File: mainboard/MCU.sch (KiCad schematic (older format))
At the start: 55 parts, among them J9 Micro_SD_Card_Det_Hirose_DM3AT, SW1 RESET, U11 STM32G474R, U12 M95256-WMN6P, U17 CD74HC4067SM, U5 MCP2562, U6 LM358

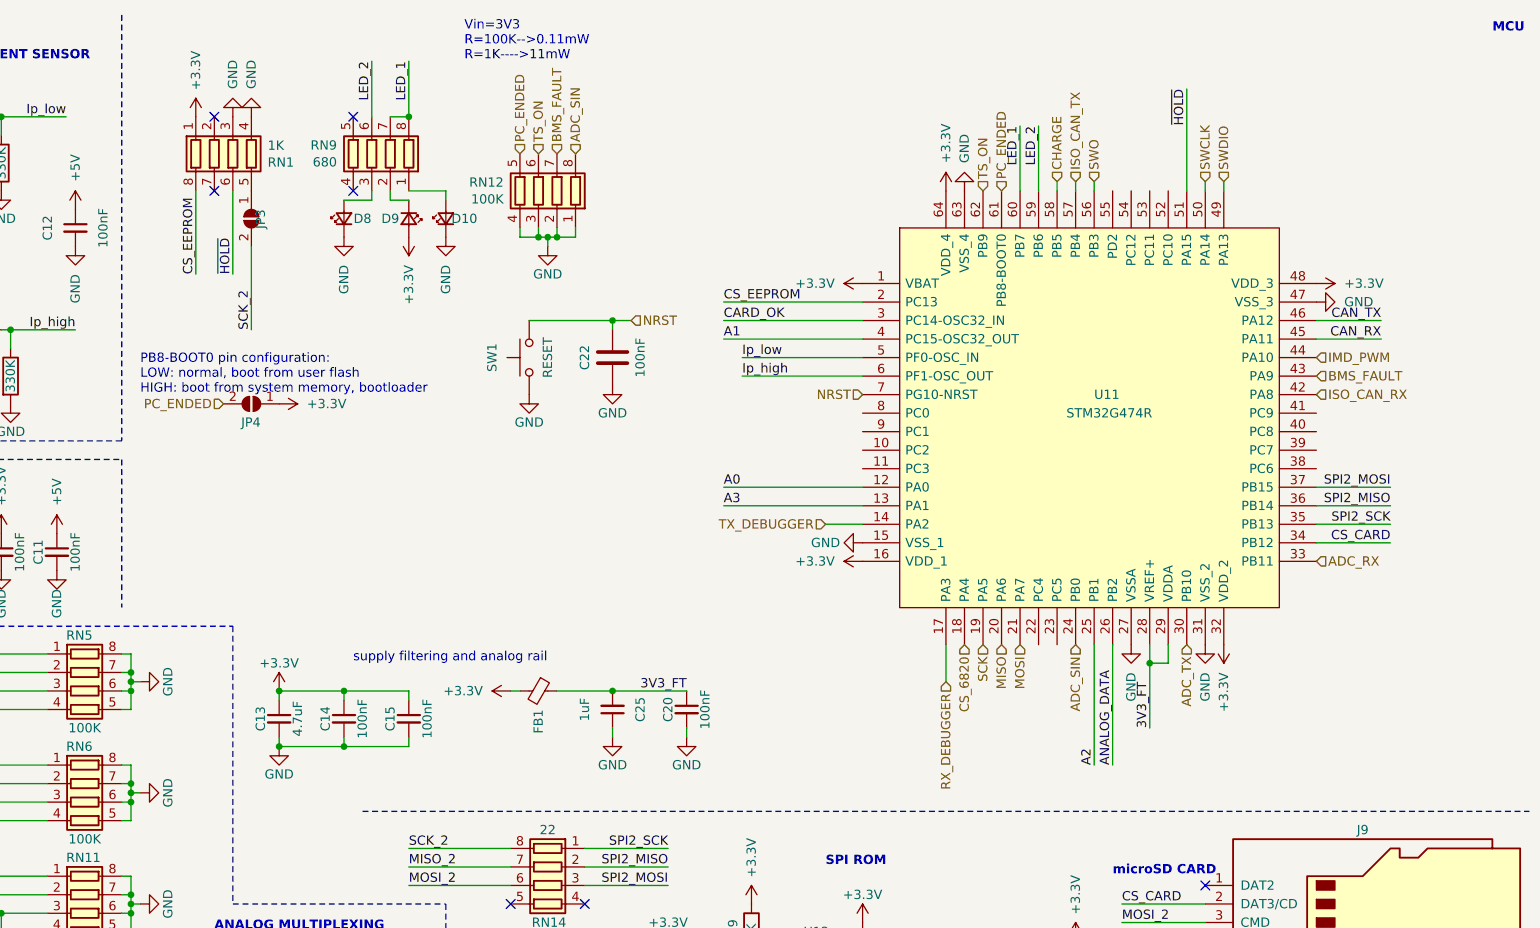
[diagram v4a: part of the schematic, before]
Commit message: 64pin, testpoints, commenting, general refactoring
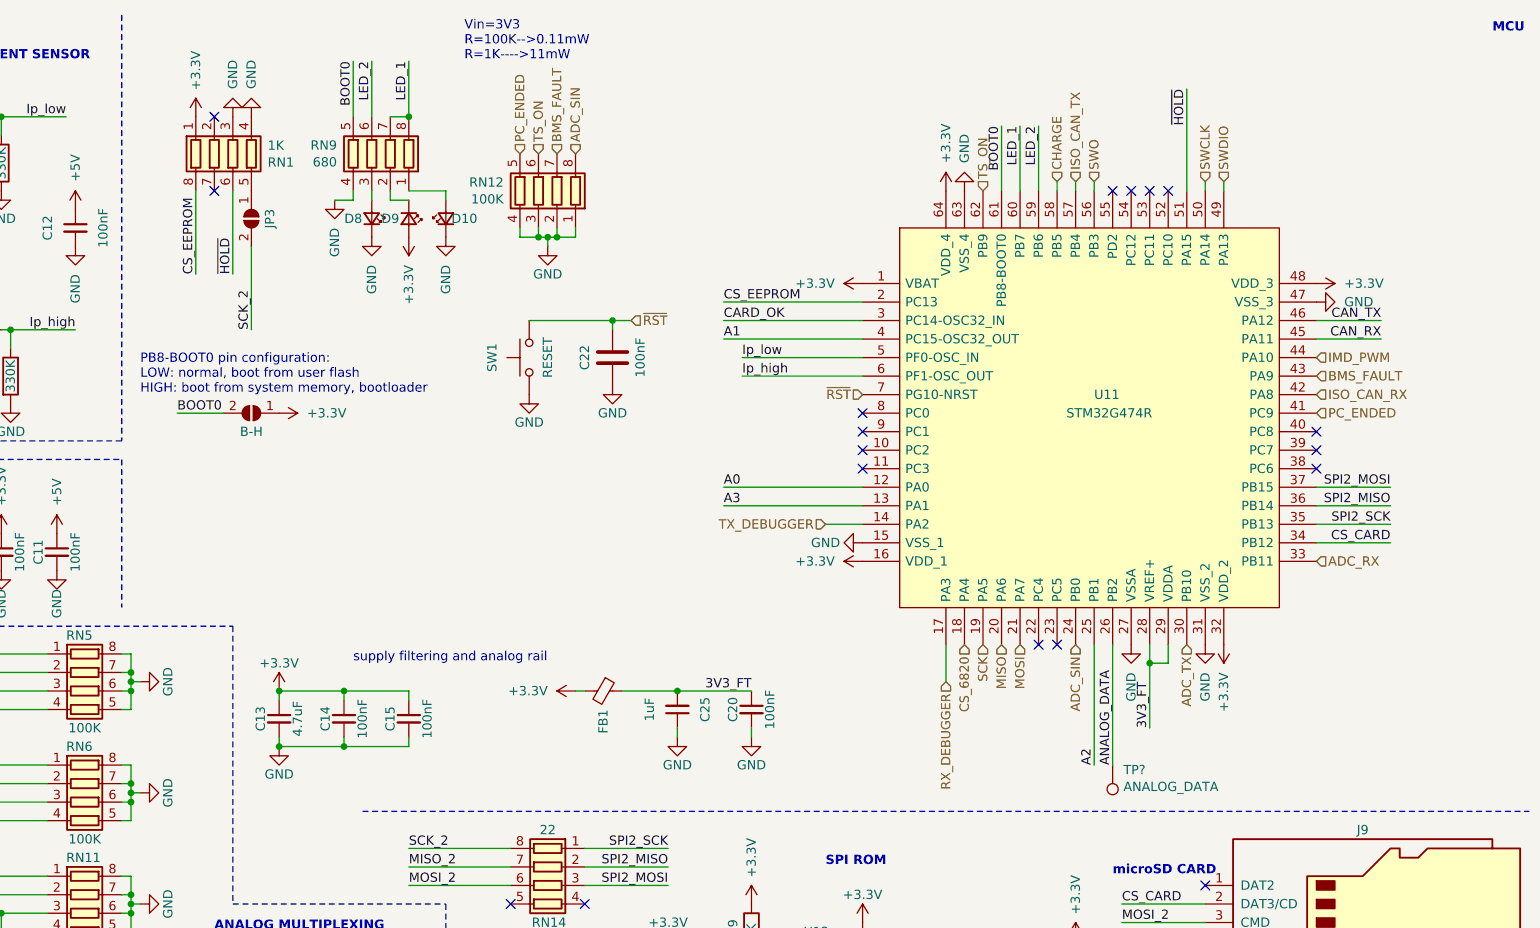
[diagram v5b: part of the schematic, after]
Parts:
- added TP?: ANALOG_DATA, symbol Connector:TestPoint
- renumbered JP4 to B-H
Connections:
- net ANALOG_DATA: now also TP?.1
- net GND: now also RN9.4 (R4.1)
- net PC_ENDED: now also U11.41 (PC9); no longer B-H.2 (B), U11.61 (PB8-BOOT0)
- net BOOT0: now reaches RN9.5 (R4.2)
- net BOOT0: now also B-H.2 (B), U11.61 (PB8-BOOT0)
- net NRST renamed ~RST~
- no-connect marks 10 -> 21
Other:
- moved on the sheet: B-H, C20, C25, D8, FB1
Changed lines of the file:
@@
 L Device:C_Small C?
 U 1 1 5E1247F7
-P 6650 4250
+P 7000 4250
 AR Path="/5E1247F7" Ref="C?"  Part="1"
 AR Path="/5DF398FB/5E1247F7" Ref="C20"  Part="1"
-F 0 "C20" V 6550 4250 50  0000 C CNN
-F 1 "100nF" V 6750 4250 50  0000 C CNN
-F 2 "Capacitor_SMD:C_0603_1608Metric" H 6688 4100 50  0001 C CNN
-F 3 "~" H 6650 4250 50  0001 C CNN
-	1    6650 4250
+F 0 "C20" V 6900 4250 50  0000 C CNN
+F 1 "100nF" V 7100 4250 50  0000 C CNN
+F 2 "Capacitor_SMD:C_0603_1608Metric" H 7038 4100 50  0001 C CNN
+F 3 "~" H 7000 4250 50  0001 C CNN
+	1    7000 4250
 	1    0    0    -1
 $EndComp
@@
 L power:GND #PWR?
 U 1 1 5DF87343
-P 6250 4400
+P 6600 4400
 AR Path="/5DF87343" Ref="#PWR?"  Part="1"
 AR Path="/5DF398FB/5DF87343" Ref="#PWR0110"  Part="1"
-F 0 "#PWR0110" H 6250 4150 50  0001 C CNN
-F 1 "GND" H 6250 4250 50  0000 C CNN
-F 2 "" H 6250 4400 50  0001 C CNN
-F 3 "" H 6250 4400 50  0001 C CNN
-	1    6250 4400
+F 0 "#PWR0110" H 6600 4150 50  0001 C CNN
+F 1 "GND" H 6600 4250 50  0000 C CNN
+F 2 "" H 6600 4400 50  0001 C CNN
+F 3 "" H 6600 4400 50  0001 C CNN
+	1    6600 4400
 	1    0    0    -1
 $EndComp
@@
 L Device:C_Small C?
 U 1 1 5DF87349
-P 6250 4250
+P 6600 4250
 AR Path="/5DF87349" Ref="C?"  Part="1"
 AR Path="/5DF398FB/5DF87349" Ref="C25"  Part="1"
-F 0 "C25" V 6100 4250 50  0000 C CNN
-F 1 "1uF" V 6400 4250 50  0000 C CNN
-F 2 "Capacitor_SMD:C_0603_1608Metric" H 6288 4100 50  0001 C CNN
-F 3 "~" H 6250 4250 50  0001 C CNN
-	1    6250 4250
+F 0 "C25" V 6450 4250 50  0000 C CNN
+F 1 "1uF" V 6750 4250 50  0000 C CNN
+F 2 "Capacitor_SMD:C_0603_1608Metric" H 6638 4100 50  0001 C CNN
+F 3 "~" H 6600 4250 50  0001 C CNN
+	1    6600 4250
 	-1   0    0    1
 $EndComp
@@
 L power:+3.3V #PWR?
 U 1 1 5E60753C
-P 5700 4150
+P 6050 4150
 AR Path="/5E60753C" Ref="#PWR?"  Part="1"
 AR Path="/5DF398FB/5E60753C" Ref="#PWR0118"  Part="1"
-F 0 "#PWR0118" H 5700 4000 50  0001 C CNN
-F 1 "+3.3V" V 5700 4300 50  0000 L CNN
-F 2 "" H 5700 4150 50  0001 C CNN
-F 3 "" H 5700 4150 50  0001 C CNN
-	1    5700 4150
+F 0 "#PWR0118" H 6050 4000 50  0001 C CNN
+F 1 "+3.3V" V 6050 4300 50  0000 L CNN
+F 2 "" H 6050 4150 50  0001 C CNN
+F 3 "" H 6050 4150 50  0001 C CNN
+	1    6050 4150
 	0    -1   -1   0
 $EndComp
@@
 L Device:FerriteBead_Small FB1
 U 1 1 5E60756E
-P 5850 4150
-F 0 "FB1" H 5950 4150 50  0000 L CNN
-F 1 "FerriteBead_Small" H 5950 4105 50  0001 L CNN
-F 2 "Inductor_SMD:L_0603_1608Metric_Pad1.05x0.95mm_HandSolder" V 5780 4150 50  0001 C CNN
-F 3 "~" H 5850 4150 50  0001 C CNN
-	1    5850 4150
+P 6200 4150
+F 0 "FB1" H 6300 4150 50  0000 L CNN
+F 1 "FerriteBead_Small" H 6300 4105 50  0001 L CNN
+F 2 "Inductor_SMD:L_0603_1608Metric_Pad1.05x0.95mm_HandSolder" V 6130 4150 50  0001 C CNN
+F 3 "~" H 6200 4150 50  0001 C CNN
+	1    6200 4150
 	0    1    1    0
 $EndComp
 Wire Wire Line
-	5950 4150 6250 4150
-Wire Wire Line
-	6250 4150 6650 4150
-Wire Wire Line
-	5700 4150 5750 4150
-Wire Wire Line
-	6250 4350 6250 4400
-Text Label 6650 4150 2    50   ~ 0
+	6300 4150 6600 4150
+Wire Wire Line
+	6600 4150 7000 4150
+Wire Wire Line
+	6050 4150 6100 4150
+Wire Wire Line
+	6600 4350 6600 4400
+Text Label 7000 4150 2    50   ~ 0
 3V3_FT
-Connection ~ 6250 4150
+Connection ~ 6600 4150
 Wire Wire Line
 	10050 2250 10400 2250
@@
 L power:GND #PWR?
 U 1 1 5E572A92
-P 6650 4400
+P 7000 4400
 AR Path="/5E572A92" Ref="#PWR?"  Part="1"
 AR Path="/5DF398FB/5E572A92" Ref="#PWR0103"  Part="1"
-F 0 "#PWR0103" H 6650 4150 50  0001 C CNN
-F 1 "GND" H 6650 4250 50  0000 C CNN
-F 2 "" H 6650 4400 50  0001 C CNN
-F 3 "" H 6650 4400 50  0001 C CNN
-	1    6650 4400
-	1    0    0    -1
-$EndComp
-Wire Wire Line
-	6650 4350 6650 4400
+F 0 "#PWR0103" H 7000 4150 50  0001 C CNN
+F 1 "GND" H 7000 4250 50  0000 C CNN
+F 2 "" H 7000 4400 50  0001 C CNN
+F 3 "" H 7000 4400 50  0001 C CNN
+	1    7000 4400
+	1    0    0    -1
+$EndComp
+Wire Wire Line
+	7000 4350 7000 4400
 Text HLabel 8250 1450 1    50   Input ~ 0
 TS_ON
@@
 L power:GND #PWR?
 U 1 1 5E86FDC4
-P 4800 1700
+P 4950 1700
 AR Path="/5E86FDC4" Ref="#PWR?"  Part="1"
 AR Path="/5DF398FB/5E86FDC4" Ref="#PWR0157"  Part="1"
-F 0 "#PWR0157" H 4800 1450 50  0001 C CNN
-F 1 "GND" V 4800 1550 50  0000 R CNN
-F 2 "" H 4800 1700 50  0001 C CNN
-F 3 "" H 4800 1700 50  0001 C CNN
-	1    4800 1700
-	1    0    0    -1
+F 0 "#PWR0157" H 4950 1450 50  0001 C CNN
+F 1 "GND" V 4950 1550 50  0000 R CNN
+F 2 "" H 4950 1700 50  0001 C CNN
+F 3 "" H 4950 1700 50  0001 C CNN
+	1    4950 1700
+	-1   0    0    -1
 $EndComp
 $Comp
 L Device:LED_Small D?
 U 1 1 5E86FDCA
-P 4800 1600
+P 4950 1600
 AR Path="/5E86FDCA" Ref="D?"  Part="1"
 AR Path="/5DF398FB/5E86FDCA" Ref="D8"  Part="1"
-F 0 "D8" V 4800 1500 50  0000 C CNN
-F 1 "LED_Small" H 4800 1744 50  0001 C CNN
-F 2 "MainBoard:LED_REVERSE_MOUNT_cilindrical" V 4800 1600 50  0001 C CNN
-F 3 "~" V 4800 1600 50  0001 C CNN
-	1    4800 1600
-	0    -1   -1   0
+F 0 "D8" V 4950 1500 50  0000 C CNN
+F 1 "LED_Small" H 4950 1744 50  0001 C CNN
+F 2 "MainBoard:LED_REVERSE_MOUNT_cilindrical" V 4950 1600 50  0001 C CNN
+F 3 "~" V 4950 1600 50  0001 C CNN
+	1    4950 1600
+	0    1    -1   0
 $EndComp
 Wire Wire Line
@@
 Wire Wire Line
 	4950 750  4950 1050
-NoConn ~ 4850 1050
-NoConn ~ 4850 1450
 $Comp
 L Device:R R?
@@
 U 1 1 5EB0119F
 P 4300 1600
-F 0 "JP3" H 4250 1550 50  0000 L CNN
+F 0 "JP3" H 4300 1500 50  0000 C CNN
 F 1 "SolderJumper_2_Open" V 4345 1648 50  0001 L CNN
 F 2 "MainBoard:Jumper_SMD_0603" H 4300 1600 50  0001 C CNN
@@
 	0    1    1    0
 $EndComp
-Wire Wire Line
-	4800 1500 4950 1500
 Wire Wire Line
 	4950 1500 4950 1450
@@
 Text Notes 3700 2550 0    50   ~ 0
 PB8-BOOT0 pin configuration:\nLOW: normal, boot from user flash\nHIGH: boot from system memory, bootloader
-Text HLabel 4150 2600 0    50   Input ~ 0
-PC_ENDED
 $Comp
 L power:+3.3V #PWR?
 U 1 1 5FD436DF
-P 4450 2600
+P 4450 2650
 AR Path="/5FD436DF" Ref="#PWR?"  Part="1"
 AR Path="/5DF398FB/5FD436DF" Ref="#PWR016"  Part="1"
-F 0 "#PWR016" H 4450 2450 50  0001 C CNN
-F 1 "+3.3V" V 4450 2750 50  0000 L CNN
-F 2 "" H 4450 2600 50  0001 C CNN
-F 3 "" H 4450 2600 50  0001 C CNN
-	1    4450 2600
+F 0 "#PWR016" H 4450 2500 50  0001 C CNN
+F 1 "+3.3V" V 4450 2800 50  0000 L CNN
+F 2 "" H 4450 2650 50  0001 C CNN
+F 3 "" H 4450 2650 50  0001 C CNN
+	1    4450 2650
 	0    1    1    0
 $EndComp
 $Comp
-L Jumper:SolderJumper_2_Open JP4
+L Jumper:SolderJumper_2_Open B-H
 U 1 1 5FD45CCD
-P 4300 2600
-F 0 "JP4" H 4250 2500 50  0000 L CNN
-F 1 "SolderJumper_2_Open" V 4345 2648 50  0001 L CNN
-F 2 "MainBoard:Jumper_SMD_0603" H 4300 2600 50  0001 C CNN
-F 3 "~" H 4300 2600 50  0001 C CNN
-	1    4300 2600
+P 4300 2650
+F 0 "B-H" H 4300 2550 50  0000 C CNN
+F 1 "SolderJumper_2_Open" V 4345 2698 50  0001 L CNN
+F 2 "MainBoard:Jumper_SMD_0603" H 4300 2650 50  0001 C CNN
+F 3 "~" H 4300 2650 50  0001 C CNN
+	1    4300 2650
 	-1   0    0    -1
 $EndComp
@@
 Wire Wire Line
 	8750 1400 8750 1450
-Text HLabel 8350 1450 1    50   Input ~ 0
+Text HLabel 10050 2650 2    50   Input ~ 0
 PC_ENDED
 Text Label 9350 900  3    50   ~ 0
@@
 $EndComp
 Text HLabel 6350 2150 2    50   Input ~ 0
-NRST
+~RST~
 Wire Wire Line
 	6250 2150 6350 2150
 Connection ~ 6250 2150
 Text HLabel 7600 2550 0    50   Input ~ 0
-NRST
+~RST~
 Text Label 10450 3350 2    50   ~ 0
 CS_CARD
@@
 Text Notes 7000 6650 0    50   ~ 0
 AMS: Automatic Moaning System
+Text Label 8350 1100 3    50   ~ 0
+BOOT0
+Wire Wire Line
+	8350 1100 8350 1450
+NoConn ~ 8950 1450
+NoConn ~ 9050 1450
+NoConn ~ 9150 1450
+NoConn ~ 9250 1450
+NoConn ~ 7600 2650
+NoConn ~ 7600 2750
+NoConn ~ 7600 2850
+NoConn ~ 7600 2950
+NoConn ~ 8550 3900
+NoConn ~ 8650 3900
+NoConn ~ 10050 2950
+NoConn ~ 10050 2750
+NoConn ~ 10050 2850
+Text Label 3900 2650 0    50   ~ 0
+BOOT0
+Wire Wire Line
+	3900 2650 4150 2650
+Text Label 4850 750  3    50   ~ 0
+BOOT0
+Wire Wire Line
+	4850 750  4850 1050
+$Comp
+L power:GND #PWR?
+U 1 1 6057F2A0
+P 4750 1500
+AR Path="/6057F2A0" Ref="#PWR?"  Part="1"
+AR Path="/5DF398FB/6057F2A0" Ref="#PWR?"  Part="1"
+F 0 "#PWR?" H 4750 1250 50  0001 C CNN
+F 1 "GND" V 4750 1350 50  0000 R CNN
+F 2 "" H 4750 1500 50  0001 C CNN
+F 3 "" H 4750 1500 50  0001 C CNN
+	1    4750 1500
+	-1   0    0    -1
+$EndComp
+Wire Wire Line
+	4750 1500 4850 1500
+Wire Wire Line
+	4850 1500 4850 1450
+$Comp
+L Connector:TestPoint TP?
+U 1 1 60590C21
+P 8950 4550
+F 0 "TP?" H 8892 4576 50  0000 R CNN
+F 1 "ANALOG_DATA" H 8892 4667 50  0000 R CNN
+F 2 "" H 9150 4550 50  0001 C CNN
+F 3 "~" H 9150 4550 50  0001 C CNN
+	1    8950 4550
+	-1   0    0    1
+$EndComp
 $EndSCHEMATC

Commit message: updated libraries
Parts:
- FB1: symbol Device:FerriteBead_Small -> Device:Ferrite_Bead_Small
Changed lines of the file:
@@
 $EndComp
 $Comp
-L Device:FerriteBead_Small FB1
+L Device:Ferrite_Bead_Small FB1
 U 1 1 5E60756E
 P 6200 4150
+AR Path="/5E60756E" Ref="FB1"  Part="1"
+AR Path="/5DF398FB/5E60756E" Ref="FB1"  Part="1"
 F 0 "FB1" H 6300 4150 50  0000 L CNN
 F 1 "FerriteBead_Small" H 6300 4105 50  0001 L CNN

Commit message: v1.1 as printed
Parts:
- removed C29: 100nF, Capacitor_SMD:C_0603_1608Metric, symbol Device:C_Small
- removed D5, D6, D7: 3V, Diode_SMD:D_SOD-323, symbol Device:D_Zener_Small
- removed R14, R15, R16: 1M, Resistor_SMD:R_0603_1608Metric, symbol Device:R
- removed R19, R20: 2K, Resistor_SMD:R_0603_1608Metric, symbol Device:R
- removed R30: 100K, Resistor_SMD:R_0603_1608Metric, symbol Device:R
- removed RN10, RN11, RN5, RN6, RN7: 100K, MainBoard:R_network_4x1_bourns_CAY16, symbol Device:R_Pack04
- removed RN14: 22, MainBoard:R_network_4x1_bourns_CAY16, symbol Device:R_Pack04
- removed RN2, RN3, RN4: 330K, MainBoard:R_network_4x1_bourns_CAY16, symbol Device:R_Pack04
- removed TP?: ANALOG_DATA, symbol Connector:TestPoint
- removed U11: STM32G474R, Package_QFP:LQFP-64_10x10mm_P0.5mm, symbol MainBoard:STM32G474R
- removed U17: CD74HC4067SM, Package_SO:TSSOP-24_4.4x7.8mm_P0.65mm, symbol 74xx:CD74HC4067SM
- added C19, C21: 1uF, Capacitor_SMD:C_0805_2012Metric, symbol Device:C_Small
- added C38, C39: 20pF, Capacitor_SMD:C_0603_1608Metric, symbol Device:C_Small
- added C48: 100nF, Capacitor_SMD:C_0603_1608Metric, symbol Device:C_Small
- added J12: SPARE_PINS, Connector_PinHeader_2.54mm:PinHeader_2x05_P2.54mm_Vertical, symbol Connector_Generic:Conn_02x05_Odd_Even
- added R6: 10K, Resistor_SMD:R_0603_1608Metric, symbol Device:R
- added RN14, RN22: 22, MainBoard:R_network_4x1_bourns_CAY16, symbol Device:R_Pack04_Split
- added TP15: Ip_high, TestPoint:TestPoint_Pad_D1.0mm, symbol Connector:TestPoint
- added TP16: BMS_FAULT, TestPoint:TestPoint_Pad_D1.0mm, symbol Connector:TestPoint
- added TP33: VCAP, TestPoint:TestPoint_Pad_D1.0mm, symbol Connector:TestPoint
- added TP9: Ip_low, TestPoint:TestPoint_Pad_D1.0mm, symbol Connector:TestPoint
- added U9: STM32F446RE_64PIN, Package_QFP:LQFP-64_10x10mm_P0.5mm, symbol MainBoard:STM32F446RE_64PIN
- added Y1: 26MHz, Crystal:Crystal_SMD_3225-4Pin_3.2x2.5mm, symbol Device:Crystal_GND24_Small
- B-H1: renamed from B-H; value SolderJumper_2_Open -> BOOT0
- C25: footprint Capacitor_SMD:C_0603_1608Metric -> Capacitor_SMD:C_0805_2012Metric
- J9: footprint MainBoard:MicroSD_Hirose_DM3AT-SF-PEJM5 -> Connector_Card:microSD_HC_Hirose_DM3AT-SF-PEJM5
- JP3: footprint MainBoard:Jumper_SMD_0603 -> Jumper:SolderJumper-2_P1.3mm_Open_RoundedPad1.0x1.5mm
- RN1: value 1K -> 100K
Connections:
- net PC_ENDED is gone; now on net BOOT0: RN12.5 (R4.2)
- net +3V3: now also RN1.2 (R2.1), C48.1, R6.1, U9.1 (VBAT), U9.19 (VDD), U9.32 (VDD), U9.48 (VDD), U9.64 (VDD)
- net 3V3_FT: now also U9.13 (VDDA)
- net ADC_RX: now also U9.25 (PC5)
- net ADC_SIN: now also U9.26 (PB0)
- net ADC_TX: now also U9.29 (PB10)
- net BMS_FAULT: now also TP16.1, U9.51 (PC10)
- net BOOT0: now also U9.60 (BOOT0); no longer RN9.5 (R4.2)
- net CAN_RX: now also RN22.5 (R4.2), U9.57 (PB5); no longer U5.4 (RXD)
- net CAN_TX: now also RN22.6 (R3.2), U9.58 (PB6I2C_1SCL); no longer U5.1 (TXD)
- net CARD_OK: now also U9.40 (PC9)
- net CHARGE: now also U9.9 (PC1/ADC)
- net CS_CARD: now also U9.39 (PC8)
- net CS_EEPROM: now also U9.37 (PC6)
- net FB_FROM_TSMS: now also U9.14 (PA0/ADC)
- net FB_IMD_FAULT: now also U9.16 (PA2)
- net FB_RELAY_LV: now also U9.15 (PA1/ADC)
- net GND: now also C19.2, C21.2, C38.2, C39.2, C48.2, J12.8 (Pin_8), U9.12 (VSSA), U9.18 (VSS), U9.31 (VSS), U9.47 (VSS), U9.63 (VSS), Y1.2, Y1.4; no longer RN9.4 (R4.1)
- net IMD_PWM: now also U9.28 (PB2)
- net ISO_CAN_RX: now also U9.44 (PA11CAN1_RX)
- net ISO_CAN_TX: now also U9.45 (PA12/CAN1_TX)
- net Ip_high: now also TP15.1, U9.11 (PC3/ADC)
- net Ip_low: now also TP9.1, U9.10 (PC2/ADC)
- net LED_1: now also U9.62 (PB9)
- net LED_2: now also U9.61 (PB8)
- net MISO_2: now also RN14.5 (R4.2)
- net MOSI_2: now also RN14.7 (R2.2)
- net SCK_2: now also RN14.6 (R3.2)
- net SPI2_MISO: now also R6.2, RN14.4 (R4.1), U9.35 (PB14)
- net SPI2_MOSI: now also RN14.2 (R2.1), U9.36 (PB15)
- net SPI2_SCK: now also RN14.3 (R3.1), U9.34 (PB13)
- net SWCLK: now also U9.49 (PA14/SWCLK)
- net SWDIO: now also U9.46 (PA13/SWD)
- net SWO: now also U9.55 (PB3)
- net TS_ON: now also U9.52 (PC11)
- net ~HOLD~: now also U9.38 (PC7)
- net ~RST~: now also U9.7 (NRST)
- net ~W~: now also RN1.7 (R2.2)
- new net: RN22.3 (R3.1), U5.1 (TXD)
- new net: RN22.4 (R4.1), U5.4 (RXD)
- new net: C19.1, C21.1, TP33.1, U9.30 (VCAP_1)
- new net: C38.1, U9.5 (PHO_OSC_IN), Y1.1
- new net: C39.1, U9.6 (PH1_OSC_OUT), Y1.3
- new net AIR+_OFF: U9.53 (PC12)
- new net AIR-_OFF: U9.54 (PD2)
- new net MUX_A0: U9.21 (PA5/SPI1SCK)
- new net MUX_A1: U9.22 (PA6/SPI1MISO)
- new net MUX_A2: U9.23 (PA7/SPI1MOSI)
- new net MUX_A3: U9.24 (PC4)
- new net MUX_OUTPUT: U9.20 (PA4/SPI1CS)
- new net PA15: J12.2 (Pin_2), U9.50 (PA15/SPI1CS)
- new net PA3: J12.7 (Pin_7), U9.17 (PA3)
- new net PA8: J12.6 (Pin_6), U9.41 (PA8)
- new net PB1: J12.5 (Pin_5), U9.27 (PB1)
- new net PB12: J12.4 (Pin_4), U9.33 (PB12)
- new net PB4: J12.1 (Pin_1), U9.56 (PB4)
- new net PB7: J12.3 (Pin_3), U9.59 (PB7/I2C_1SDA)
- new net PC0: J12.9 (Pin_9), U9.8 (PC0/ADC)
- new net PC13: J12.10 (Pin_10), U9.2 (PC13)
- new net RX_SWD: U9.43 (PA10)
- new net TX_SWD: U9.42 (PA9)
- no-connect marks 21 -> 6
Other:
- note added: "AMS: Accumulator Management System"
- note removed: "AMS: Automatic Moaning System"
- note removed: "ANALOG MULTIPLEXING"
- note removed: "I=12V/430K=2.79*10^(-5)\nR=330K-->0.26mW\nR=100K-->0.078mW"
- note removed: "Step down"
- note removed: "Vin=3V3\nR=100K-->0.11mW\nR=1K---->11mW"
- note removed: "Zeners for voltage clamping"
- note removed: "current into R14-R16\nif Vsd=12V--->9uA\nif Vsd=55V--->52uA"
- moved on the sheet: C10, C11, C13, C14, C15, C20, C22, C25, D10, D8, D9, FB1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
